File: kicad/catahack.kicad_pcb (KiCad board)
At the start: 4 copper layers, 100 x 100 mm, 178 parts, among them J1 XCVR power choice, J10 PC_AUDIO_EXTRA, J11 Jack header, J12 Jack header, J13 L/R channel choice, J14 Jack header, J15 CITA/OMTP choice, J16 TRRS/TRS+TS choice, J18 Xcvr grounding jumpers, J19 XCVR_Audio, J2 USB_B, J3 FTDI header, J4 PTT choice, J5 XCVR_CAT_TTL, J6 XCVR_PTT, J7 XCVR_CAT_RS232, J8 PC_AUDIO_IO, J9 PC_AUDIO_OUT, T1 T6003NL, T2 T6003NL, U1 PQS075-S5-S5-S, U2 L78M05CDT-TR, U3 SN65220, U4 Si8663AB-B-IS1, U5 FT232RL, U6 SN74HCT32D, U7 VOR1121B6T, U8 MAX3387ECUG+

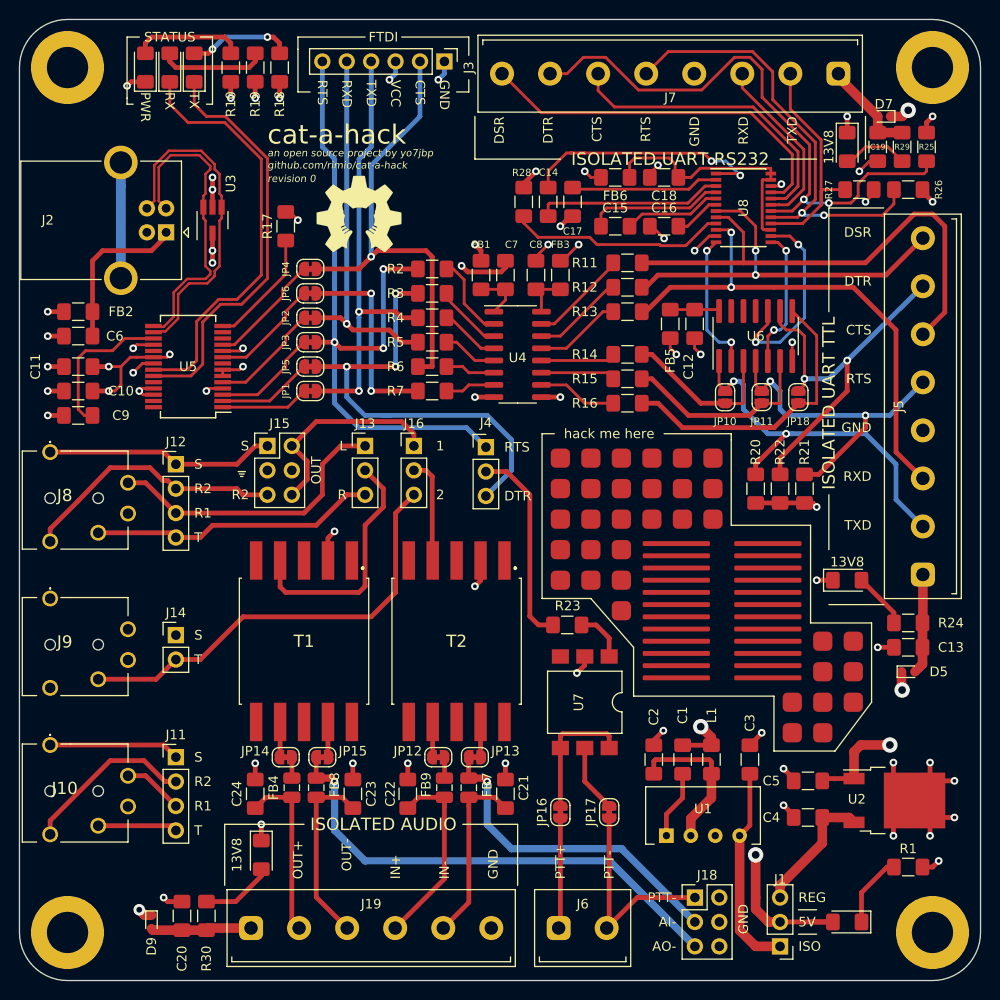
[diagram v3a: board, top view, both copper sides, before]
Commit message: Ferrite beads, hacking pads, audio fix
* Chose ferrite beads for IC Vcc (BLM31KN102SH1L)
* Change hacking pad thickness to 0.8mm
* Fixed potential oscillator when grounding audio- lines
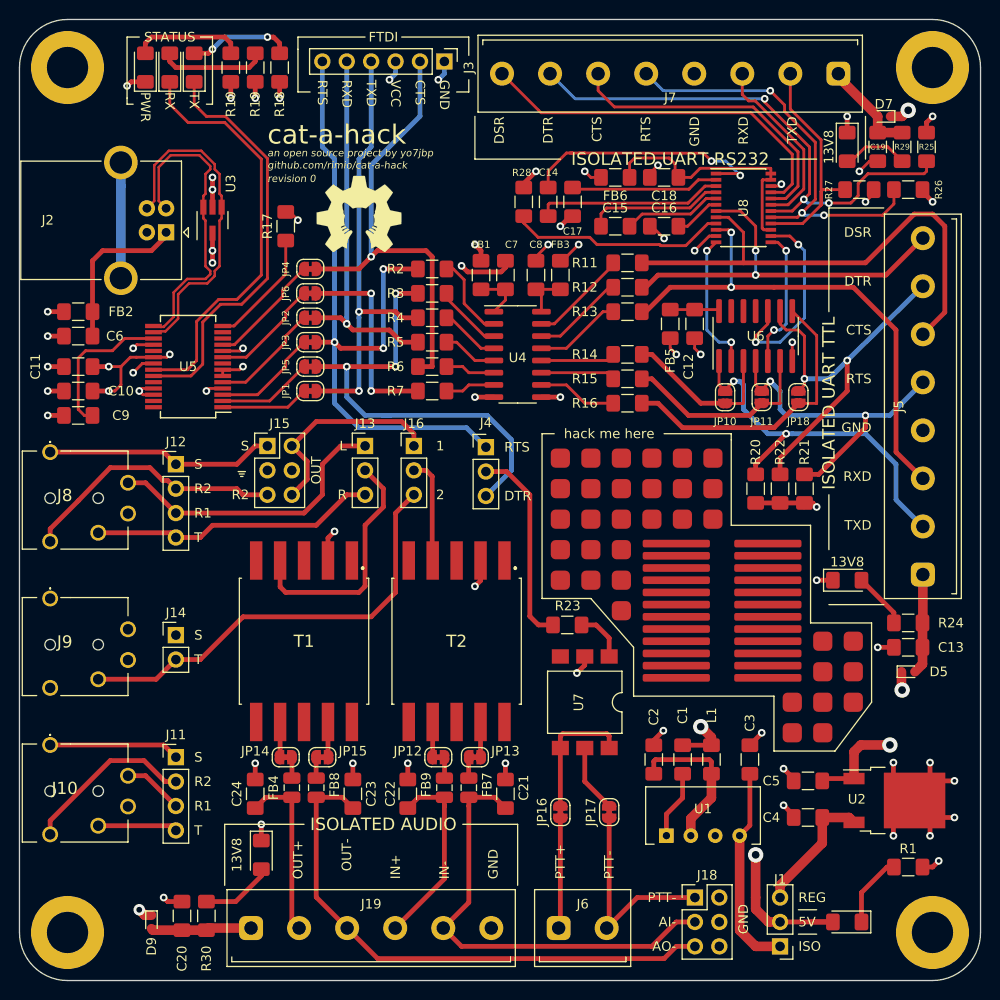
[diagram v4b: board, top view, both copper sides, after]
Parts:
- removed the REF** at (102.9, 103.5)
- removed the REF** at (93.3, 97.2)
- removed the REF** at (93.3, 95.9)
- removed the REF** at (102.9, 97.2)
- removed the REF** at (93.3, 98.4)
- removed the REF** at (102.9, 94.6)
- removed the REF** at (93.3, 94.6)
- removed the REF** at (102.9, 95.9)
- removed the REF** at (102.9, 93.3)
- removed the REF** at (93.3, 93.3)
- removed the REF** at (102.9, 92.1)
- removed the REF** at (93.3, 102.2)
- removed the REF** at (93.3, 92.1)
- removed the REF** at (102.9, 90.8)
- removed the REF** at (93.3, 90.8)
- removed the REF** at (102.9, 89.5)
- removed the REF** at (93.3, 89.5)
- removed the REF** at (93.3, 101.0)
- removed the REF** at (102.9, 102.2)
- removed the REF** at (93.3, 103.5)
- removed the REF** at (102.9, 99.7)
- removed the REF** at (93.3, 99.7)
- removed the REF** at (102.9, 101.0)
- removed the REF** at (102.9, 98.4)
- added REF**: Generic_Pad_SOP_7x0.8mm, custom:Generic_Pad_SOP_7x0.8mm, F.Cu at (93.3, 103.5)
- added REF**: Generic_Pad_SOP_7x0.8mm, custom:Generic_Pad_SOP_7x0.8mm, F.Cu at (102.9, 98.4)
- added REF**: Generic_Pad_SOP_7x0.8mm, custom:Generic_Pad_SOP_7x0.8mm, F.Cu at (93.3, 97.2)
- added REF**: Generic_Pad_SOP_7x0.8mm, custom:Generic_Pad_SOP_7x0.8mm, F.Cu at (102.9, 97.2)
- added REF**: Generic_Pad_SOP_7x0.8mm, custom:Generic_Pad_SOP_7x0.8mm, F.Cu at (93.3, 95.9)
- added REF**: Generic_Pad_SOP_7x0.8mm, custom:Generic_Pad_SOP_7x0.8mm, F.Cu at (102.9, 95.9)
- added REF**: Generic_Pad_SOP_7x0.8mm, custom:Generic_Pad_SOP_7x0.8mm, F.Cu at (93.3, 94.6)
- added REF**: Generic_Pad_SOP_7x0.8mm, custom:Generic_Pad_SOP_7x0.8mm, F.Cu at (102.9, 94.6)
- added REF**: Generic_Pad_SOP_7x0.8mm, custom:Generic_Pad_SOP_7x0.8mm, F.Cu at (93.3, 93.3)
- added REF**: Generic_Pad_SOP_7x0.8mm, custom:Generic_Pad_SOP_7x0.8mm, F.Cu at (102.9, 93.3)
- added REF**: Generic_Pad_SOP_7x0.8mm, custom:Generic_Pad_SOP_7x0.8mm, F.Cu at (93.3, 92.1)
- added REF**: Generic_Pad_SOP_7x0.8mm, custom:Generic_Pad_SOP_7x0.8mm, F.Cu at (102.9, 103.5)
- added REF**: Generic_Pad_SOP_7x0.8mm, custom:Generic_Pad_SOP_7x0.8mm, F.Cu at (102.9, 92.1)
- added REF**: Generic_Pad_SOP_7x0.8mm, custom:Generic_Pad_SOP_7x0.8mm, F.Cu at (93.3, 90.8)
- added REF**: Generic_Pad_SOP_7x0.8mm, custom:Generic_Pad_SOP_7x0.8mm, F.Cu at (102.9, 90.8)
- added REF**: Generic_Pad_SOP_7x0.8mm, custom:Generic_Pad_SOP_7x0.8mm, F.Cu at (102.9, 89.5)
- added REF**: Generic_Pad_SOP_7x0.8mm, custom:Generic_Pad_SOP_7x0.8mm, F.Cu at (93.3, 89.5)
- added REF**: Generic_Pad_SOP_7x0.8mm, custom:Generic_Pad_SOP_7x0.8mm, F.Cu at (93.3, 102.2)
- added REF**: Generic_Pad_SOP_7x0.8mm, custom:Generic_Pad_SOP_7x0.8mm, F.Cu at (102.9, 102.2)
- added REF**: Generic_Pad_SOP_7x0.8mm, custom:Generic_Pad_SOP_7x0.8mm, F.Cu at (93.3, 101.0)
- added REF**: Generic_Pad_SOP_7x0.8mm, custom:Generic_Pad_SOP_7x0.8mm, F.Cu at (102.9, 101.0)
- added REF**: Generic_Pad_SOP_7x0.8mm, custom:Generic_Pad_SOP_7x0.8mm, F.Cu at (93.3, 99.7)
- added REF**: Generic_Pad_SOP_7x0.8mm, custom:Generic_Pad_SOP_7x0.8mm, F.Cu at (102.9, 99.7)
- added REF**: Generic_Pad_SOP_7x0.8mm, custom:Generic_Pad_SOP_7x0.8mm, F.Cu at (93.3, 98.4)
- FB1, FB2, FB3, FB5, FB6: value Fe -> BLM31KN102SH1L
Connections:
- J18 pad 3: Net-(FB7-Pad2) -> Net-(C21-Pad1)
- J18 pad 5: Net-(FB8-Pad2) -> Net-(C23-Pad1)
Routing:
- net Net-(FB8-Pad2): track 51.8 -> 2.18 mm, vias 1 -> 0
- net Net-(C23-Pad1): track 19.2 -> 57.2 mm
- net Net-(FB7-Pad2): track 34.5 -> 2.18 mm, vias 1 -> 0
- net Net-(C21-Pad1): track 19.0 -> 47.0 mm
- net /data/rs232/RS232_DTR: track 62.0 -> 56.1 mm, vias 2 -> 3
- net /data/rs232/RS232_RTS: track 47.2 -> 43.9 mm, vias 2 -> 3

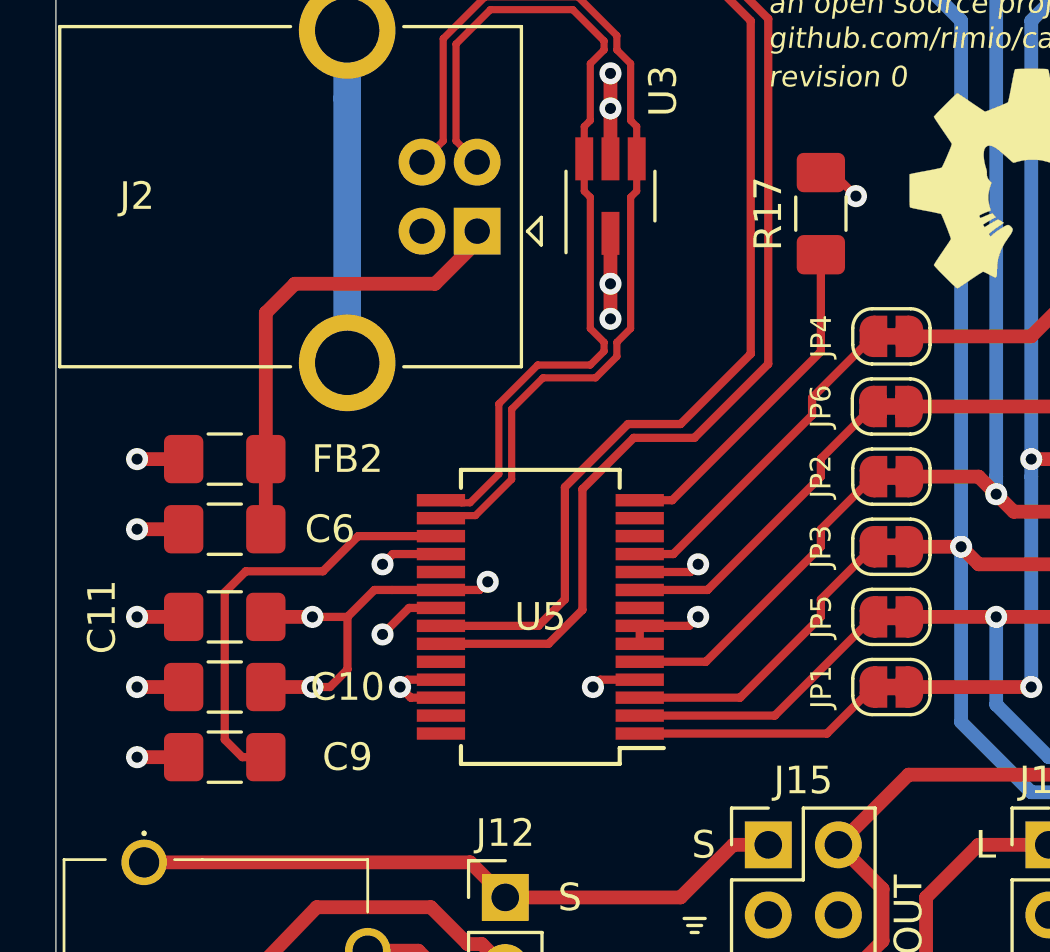
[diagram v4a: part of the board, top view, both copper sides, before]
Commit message: Removed extra bypass cap from USB VBUS pin due to closeness to FTDI bypass cap; rerouted some traces
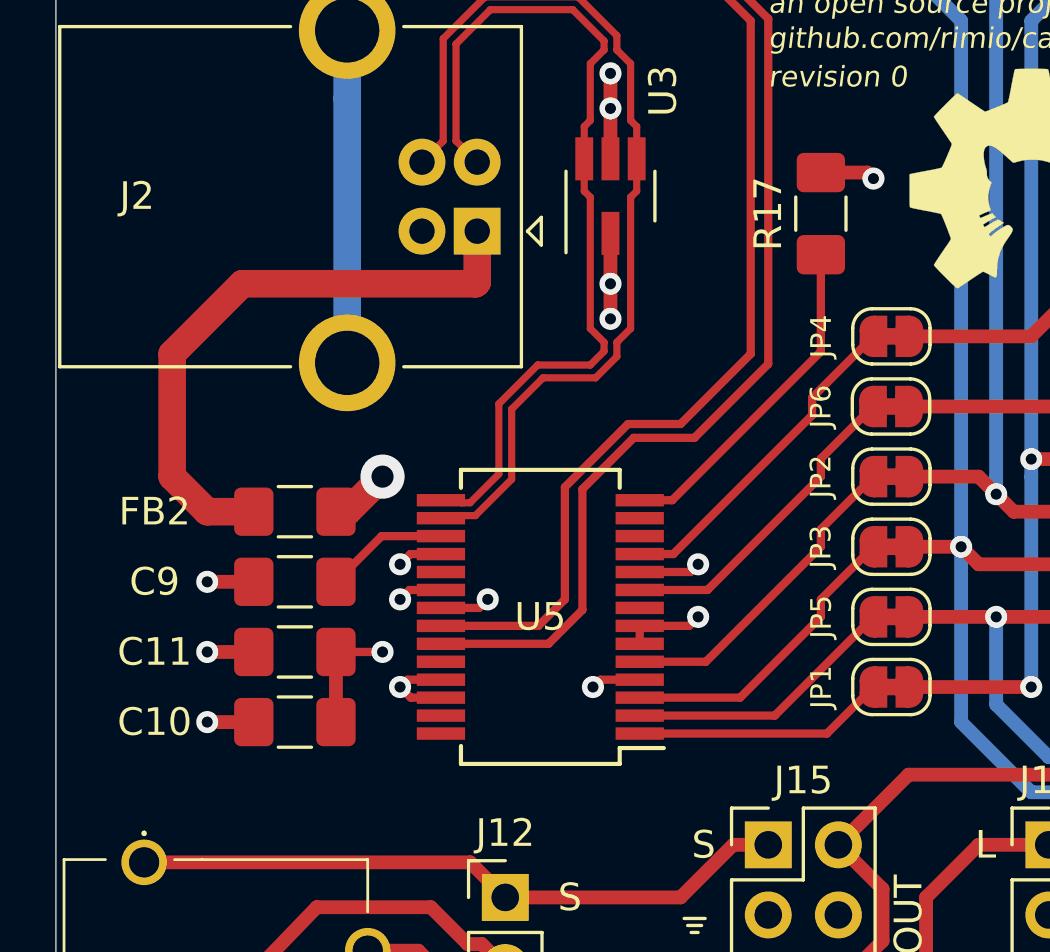
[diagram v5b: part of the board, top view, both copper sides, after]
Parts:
- removed C6: 10n, Capacitor_SMD:C_1206_3216Metric_Pad1.42x1.75mm_HandSolder
- moved C9 6.84 mm to (33.7, 69.8)
- moved FB2 3.18 mm to (33.7, 67.3), turned to 180 degrees
- moved C10 2.84 mm to (33.7, 74.9)
- moved C11 2.84 mm to (33.7, 72.4)
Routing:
- net Net-(C9-Pad1): track 15.8 -> 4.49 mm
- net VCC: track 33.4 -> 26.4 mm, vias 12 -> 11
- net Net-(FB2-Pad2): track 16.9 -> 21.9 mm
- net GND: track 49.2 -> 46.2 mm, vias 19 -> 18

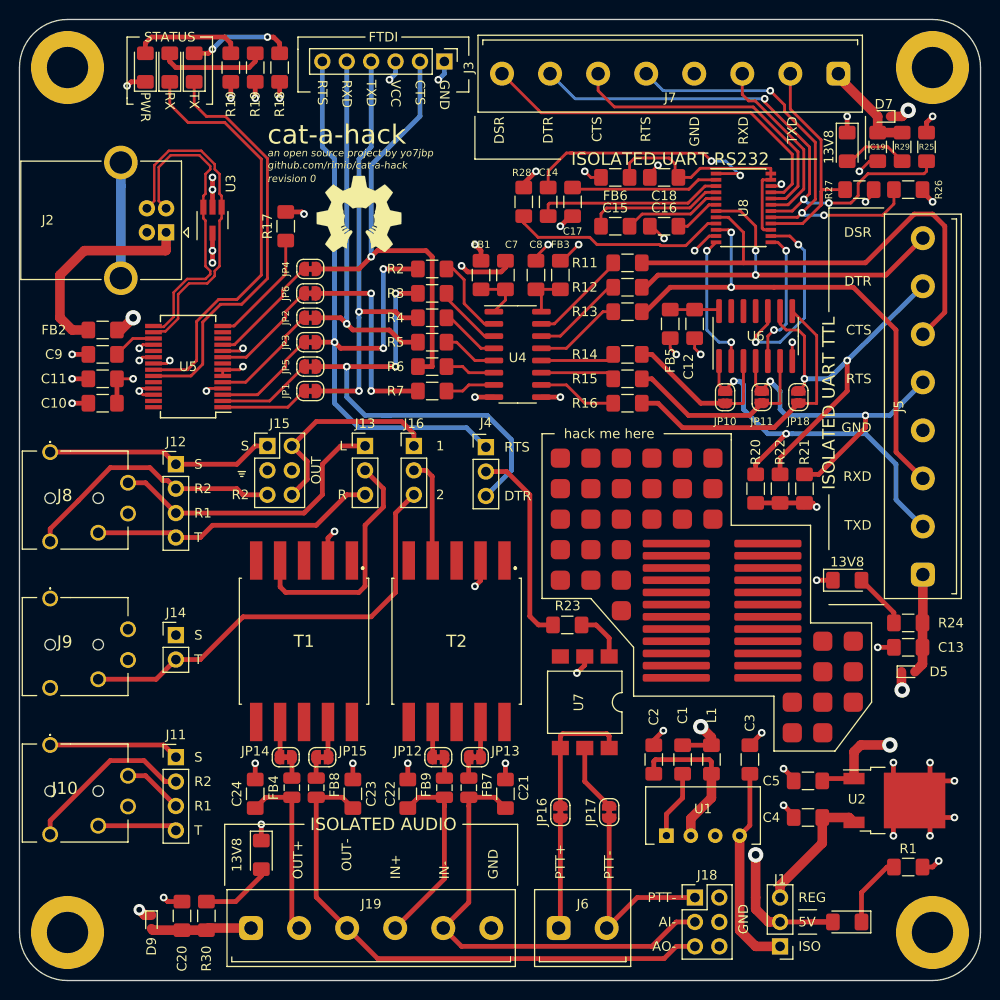
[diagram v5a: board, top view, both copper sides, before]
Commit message: Small fixes
* Moved via that was unreasonably close to another one
* Changed 13V8 diodes to SM5819PL-TP
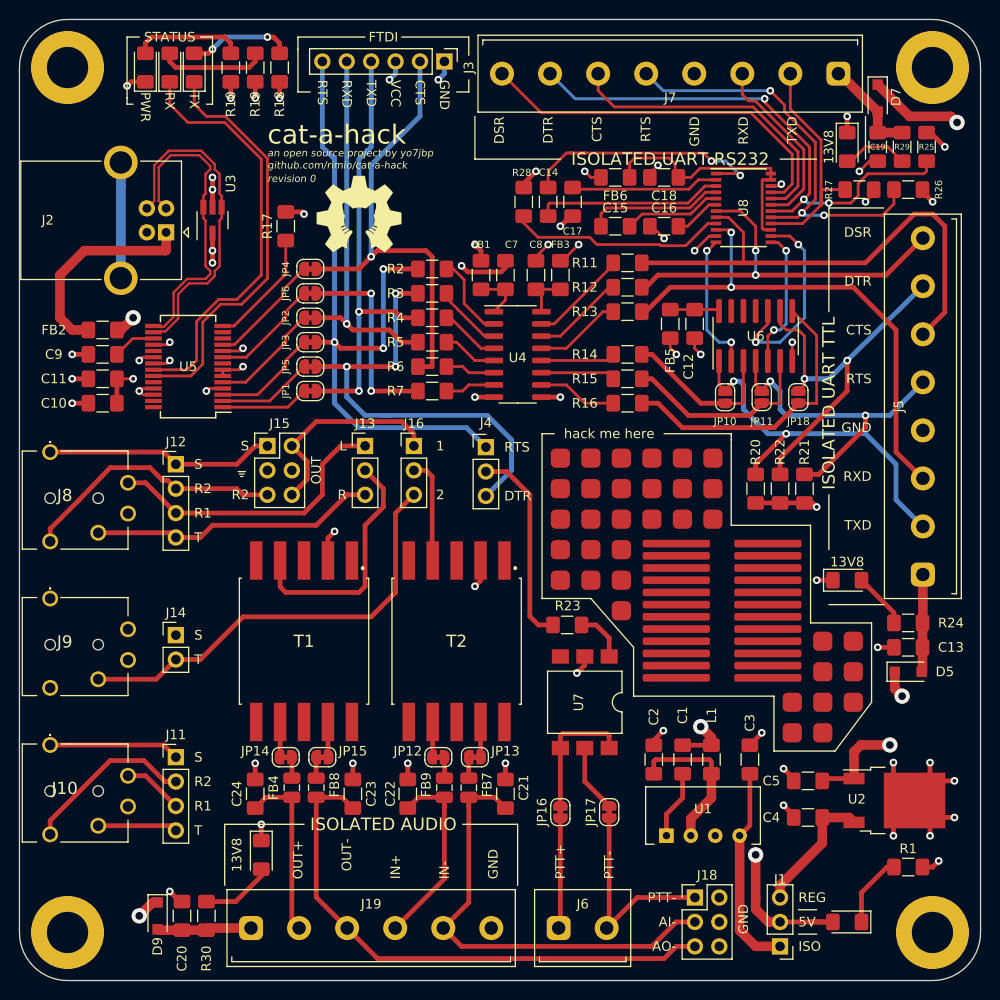
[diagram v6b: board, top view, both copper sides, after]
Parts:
- D5, D7, D9: value 1N4148X-TP -> SM5819PL-TP; footprint Diode_SMD:D_SOD-523 -> Diode_SMD:D_SOD-123F
- moved D7 2.01 mm to (114.3, 43.2), turned to 270 degrees
- moved D9 0.90 mm to (39.4, 128.3)
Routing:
- net XCVR_13V8: track 15.8 -> 25.4 mm, vias 7 -> 4
- net Net-(C20-Pad1): track 10.5 -> 9.85 mm

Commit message: Bugfixes
* Fixed USB D+/D- switch
* Added clearance at top right mounting hole
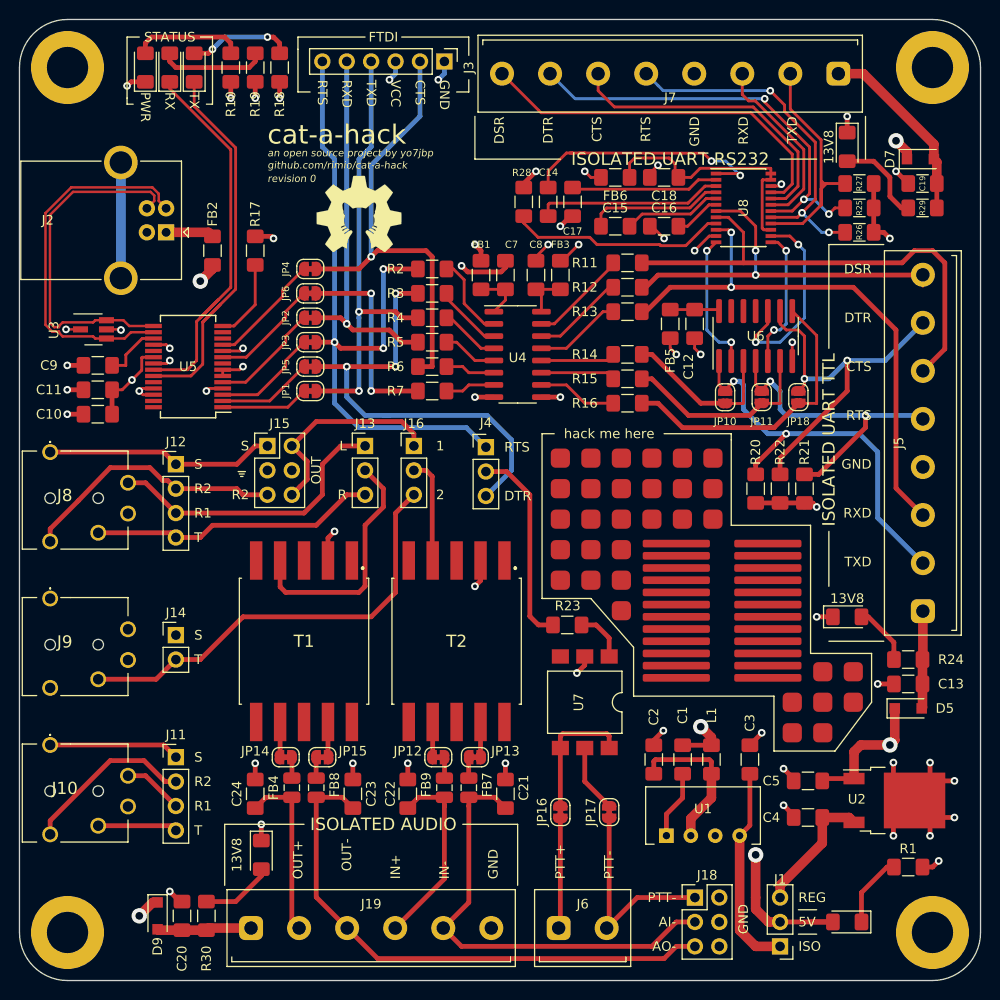
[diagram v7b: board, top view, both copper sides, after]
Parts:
- removed the REF** at (108.6, 99.7)
- removed the REF** at (111.8, 99.7)
- moved U3 16.8 mm to (32.7, 67.2), turned to 0 degrees
- moved FB2 14.1 mm to (45.1, 59.1), turned to 90 degrees
- moved R25 9.44 mm to (112.4, 54.6), turned to 0 degrees
- moved D7 7.75 mm to (118.7, 49.5), turned to 0 degrees
- moved R26 6.75 mm to (112.4, 57.1)
- moved R29 6.70 mm to (119.0, 54.6), turned to 180 degrees
- moved C19 6.02 mm to (119.0, 52.1), turned to 180 degrees
- moved R17 4.07 mm to (49.5, 59.1)
- moved C13 3.81 mm to (117.5, 104.1)
- moved D5 3.81 mm to (117.5, 106.7)
- moved D6 3.81 mm to (111.1, 97.2)
- moved J5 3.81 mm to (119.0, 79.1)
- moved R24 3.81 mm to (117.5, 101.6)
- moved C11 1.25 mm to (33.1, 73.5)
- moved C9 1.25 mm to (33.1, 71.0)
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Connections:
- J2 pad 2: USB_D+ -> USB_D-
- J2 pad 3: USB_D- -> USB_D+
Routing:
- net Net-(FB2-Pad2): track 21.9 -> 5.00 mm
- net /data/rs232/RS232_DTR: track 56.1 -> 45.2 mm
- net Net-(C19-Pad1): track 10.5 -> 19.7 mm
- net XCVR_13V8: track 25.4 -> 19.1 mm, vias 4 -> 3
- net /data/rs232/RS232_RTS: track 43.9 -> 37.6 mm
- net USB_D-: track 34.8 -> 38.8 mm
- net USB_D+: track 32.5 -> 36.5 mm
- net Net-(R17-Pad2): track 12.3 -> 8.44 mm
- net XCVR_RXD: track 53.4 -> 57.2 mm
- net /data/XCVR_TXD_CON: track 39.9 -> 43.3 mm
- net RXLED: track 44.0 -> 40.7 mm
- net VCC: track 26.4 -> 29.6 mm, vias 11 -> 10
- net GND: track 46.4 -> 43.3 mm, vias 18 -> 16
- net Net-(D8-Pad2): track 6.95 -> 9.53 mm
- net TXLED: track 43.4 -> 40.8 mm
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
